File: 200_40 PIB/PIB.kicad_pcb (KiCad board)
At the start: 2 copper layers, 80 x 49 mm, 110 parts, among them Q1 3300V, Q3 VO3120, Q6 ?, Q7 ?, T2 Arthur, T3 Arthur, U2 L298N, U4 LM5022MM, U5 LTV-817-C, U6 TLVH431BQDCKT, U7 LM5022MM, U8 LTV-817-C, U9 TLVH431BQDCKT

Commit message: intermediate pib work, add history to gitignore
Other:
- board size 80 x 49 mm -> 18.3 x 25.4 mm
- board text added: "For Instructional Use Only."
- board text added: "SOLIDWORKS Educational Product."

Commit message: pretty pib that doesnt work
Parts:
- removed A1: Arduino_Nano_v3.x, Module:Arduino_Nano
- removed C1: 0.47uF, Capacitor_THT:C_Rect_L41.5mm_W13.0mm_P37.50mm_MKS4
- removed C26, C39: 100nF, Capacitor_SMD:C_2220_5750Metric
- removed Q1: 3300V, Package_TO_SOT_THT:TO-247-4_Horizontal_TabDown
- removed Q6, Q7: ?, Package_TO_SOT_THT:TO-247-4_Horizontal_TabDown
- removed T2, T3: Arthur, PlanarTransformer:40-2Transformer
- removed TP15, TP16, TP17, TP18, TP19, TP20, TP21, TP22, TP23, TP24, TP25, TP26, TP27, TP28, TP29, TP30, TP31, TP32, TP33, TP34, TP35, TP36, TP37, TP38, TP39, TP40, TP41, TP42, TP43, TP44: 5004, TestPoint:TestPoint_Keystone_5000-5004_Miniature
- removed U2: L298N, Package_TO_SOT_THT:TO-220-15_P2.54x5.08mm_StaggerOdd_Lead4.58mm_Vertical
- added J3: PIB Interface, Connector_Harwin:Harwin_Gecko_G125-MS12605M2P_2x13_P1.25mm_Vertical, F.Cu at (190.2, 112.7)
- added Q2: EPC2302, EPC_FETs:D0606F_100V, B.Cu at (221.0, 128.5)
- added Q4: EPC2302, EPC_FETs:D0606F_100V, B.Cu at (205.9, 128.6)
- added Q8: IRF7403, Package_SO:SOIC-8_3.9x4.9mm_P1.27mm, B.Cu at (209.5, 106.0)
- added Q9: IRF7403, Package_SO:SOIC-8_3.9x4.9mm_P1.27mm, B.Cu at (209.5, 100.5)
- added REF**: Transformer_NF_ETAL_P1165, Transformer_THT:Transformer_NF_ETAL_P1165, F.Cu at (230.0, 123.5)
- added REF**: TO-247-4_Horizontal_TabUp, Package_TO_SOT_THT:TO-247-4_Horizontal_TabUp, B.Cu at (244.6, 113.6)
- added REF**: Molex_PicoBlade_53261-0671_1x06-1MP_P1.25mm_Horizontal, Connector_Molex:Molex_PicoBlade_53261-0671_1x06-1MP_P1.25mm_Horizontal, F.Cu at (222.6, 94.7)
- added REF**: Transformer_NF_ETAL_P1165, Transformer_THT:Transformer_NF_ETAL_P1165, F.Cu at (209.5, 123.5)
- added REF**: MountingHole_3.2mm_M3_DIN965_Pad, MountingHole:MountingHole_3.2mm_M3_DIN965_Pad, F.Cu at (190.0, 130.5)
- added REF**: HARWIN_M80-5100442, PIB_Footprint_Library:HARWIN_M80-5100442, F.Cu at (207.0, 95.0)
- added REF**: MountingHole_3.2mm_M3_DIN965_Pad, MountingHole:MountingHole_3.2mm_M3_DIN965_Pad, F.Cu at (255.5, 137.0)
- added REF**: MountingHole_3.2mm_M3_DIN965_Pad, MountingHole:MountingHole_3.2mm_M3_DIN965_Pad, F.Cu at (196.5, 95.0)
- added REF**: Molex_PicoBlade_53261-0671_1x06-1MP_P1.25mm_Horizontal, Connector_Molex:Molex_PicoBlade_53261-0671_1x06-1MP_P1.25mm_Horizontal, F.Cu at (263.0, 125.5)
- added REF**: MountingHole_3.2mm_M3_DIN965_Pad, MountingHole:MountingHole_3.2mm_M3_DIN965_Pad, F.Cu at (256.5, 95.0)
- added U10: TLP3543, Package_DIP:DIP-6_W7.62mm, F.Cu at (247.7, 109.5)
- added U11: STM32G431KBTx, Package_QFP:LQFP-32_7x7mm_P0.8mm, F.Cu at (202.0, 106.5)
- added U12: DRV8220DRL, Package_TO_SOT_SMD:SOT-563, F.Cu at (209.5, 107.0)
- added U13: DRV8220DRL, Package_TO_SOT_SMD:SOT-563, F.Cu at (209.5, 103.5)
- added U3: BDJ2FC0WEFJ, Package_SO:HTSOP-8-1EP_3.9x4.9mm_P1.27mm_EP2.4x3.2mm, F.Cu at (216.5, 105.1)
- C16, C17, C18, C20, C22, C23, C24, C35, C36, C37, D4, D6, D7, D9, R17, R19, R22, R23, R24, R25, R33, R40, R43, R47, U4, U7: moved to B.Cu
- U1: value ~ -> ACS37042KLHBLT-030B3; footprint Package_SO:TSSOP-20_4.4x6.5mm_P0.65mm -> Package_TO_SOT_SMD:SOT-23-5_HandSoldering
- moved R29 188.1 mm to (260.2, 109.6)
- moved R20 181.4 mm to (260.1, 113.3), turned to 90 degrees
- moved R21 179.9 mm to (258.0, 113.3), turned to 90 degrees
- moved R30 158.2 mm to (259.5, 100.5)
- moved D5 151.8 mm to (231.5, 101.0), turned to 90 degrees
- moved R31 151.8 mm to (251.5, 100.5)
- moved Q3 151.0 mm to (242.8, 101.7), turned to -90 degrees
- moved U6 142.4 mm to (226.0, 100.5), turned to 90 degrees
- moved C19 139.9 mm to (246.0, 94.5), turned to 90 degrees
- moved C21 137.1 mm to (242.5, 94.5), turned to 90 degrees
- moved U5 128.6 mm to (231.7, 93.7)
- moved R36 126.4 mm to (245.4, 99.0)
- moved C15 123.0 mm to (230.2, 111.6)
- moved R35 122.1 mm to (242.0, 99.0)
- moved C14 118.5 mm to (225.5, 111.6)
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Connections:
- net /+18V_ISO renamed /+20V_ISO
- Q3 pad 2: /FIRE -> unconnected-(Q3-A-Pad2)
- Q3 pad 3: GNDPWR -> unconnected-(Q3-C-Pad3)
- R16 pad 2: Net-(U4-UVLO) -> /Igniter Supply/EN
- R18 pad 1: Net-(U4-UVLO) -> /Igniter Supply/EN
- U1 pad 1: unconnected-(U1-AV_DD-Pad1) -> GNDREF
- U1 pad 2: GNDPWR -> /I_IG
- U1 pad 3: unconnected-(U1-REFIN--Pad3) -> +3.3V
- U1 pad 4: unconnected-(U1-REFIN+/OUT-Pad4) -> /I_IG
- U1 pad 5: unconnected-(U1-CH0-Pad5) -> GNDPWR
- U4 pad 7: Net-(U4-UVLO) -> /Igniter Supply/EN
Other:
- board size 18.3 x 25.4 mm -> 80 x 49 mm
- board text removed: "For Instructional Use Only."
- board text removed: "SOLIDWORKS Educational Product."

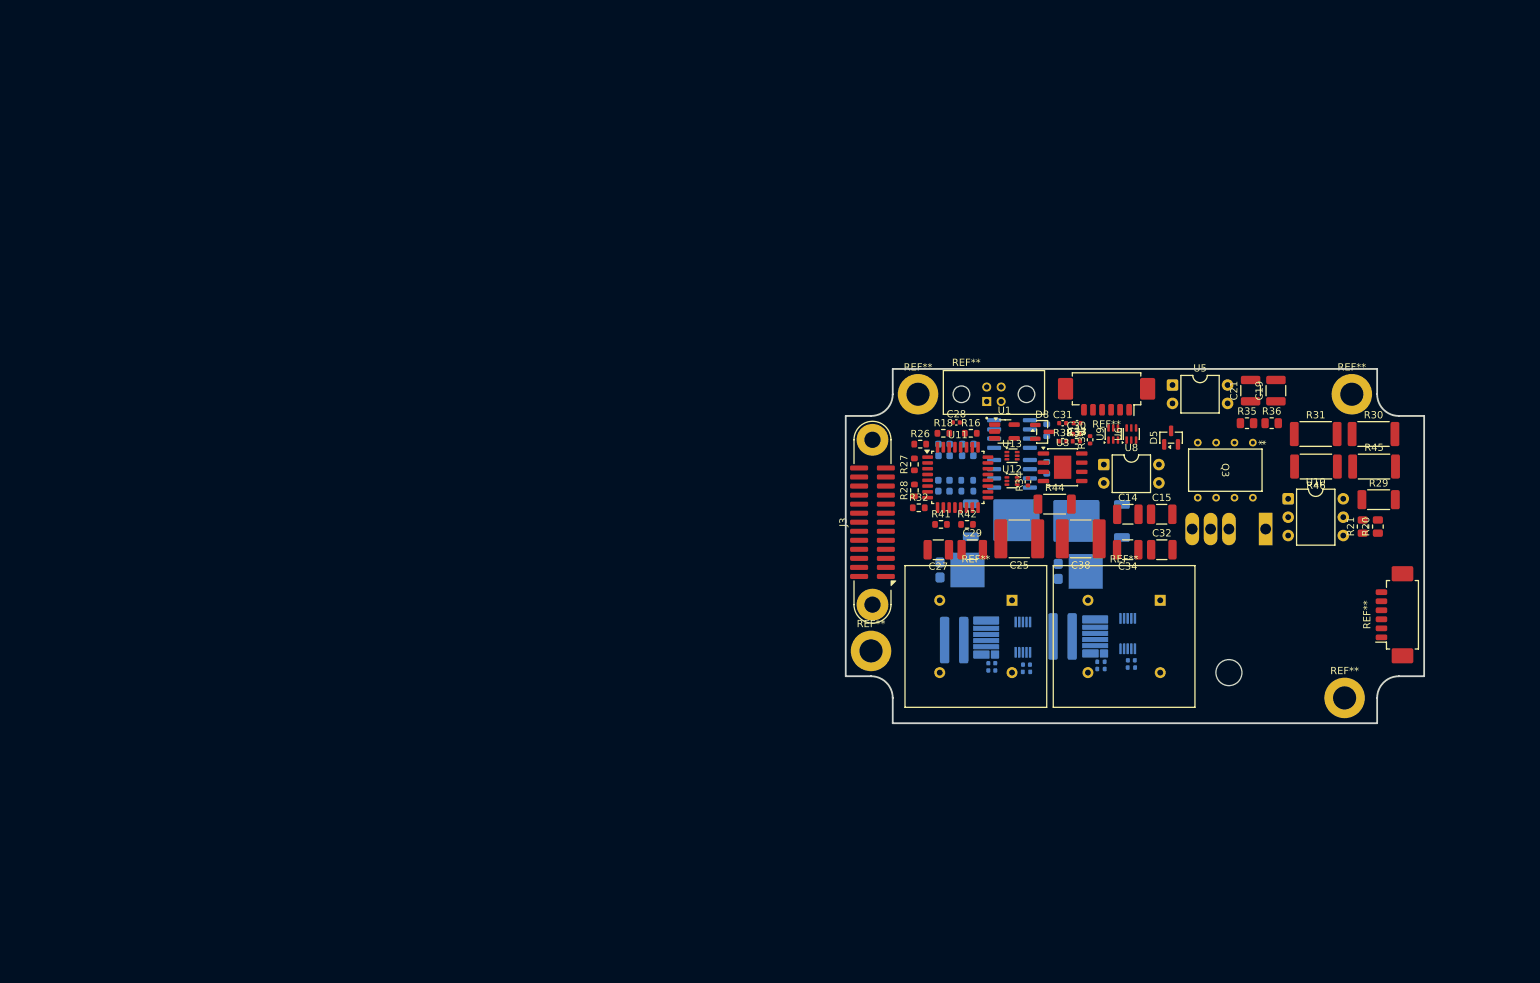
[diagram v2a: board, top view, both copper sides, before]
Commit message: assign PIB footprints, push ioc file to CubeMX 6.18.1
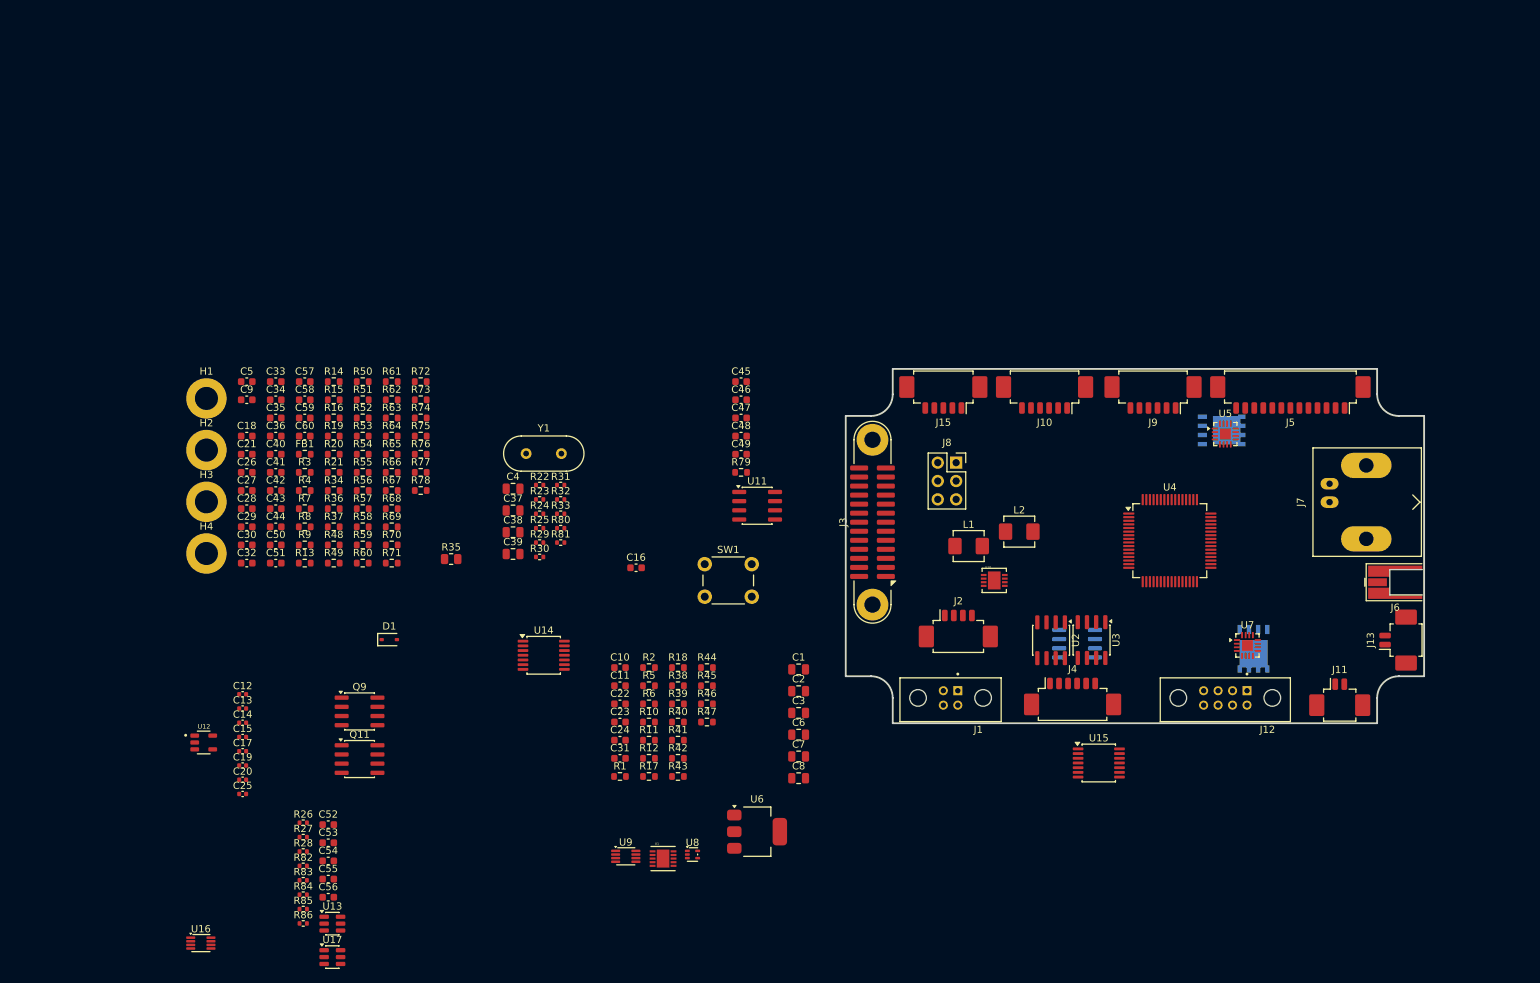
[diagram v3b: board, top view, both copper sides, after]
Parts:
- removed D4, D7: PPH10100, Package_TO_SOT_SMD:TO-277A
- removed D5, D8: BZX84C12, Package_TO_SOT_SMD:SOT-23
- removed D6, D9: VS-8EWS16STR-M3, Package_TO_SOT_SMD:TO-252-2
- removed Q3: VO3120, PIB_Footprint_Library:DIP_3120_VIS
- removed Q4: EPC2302, EPC_FETs:D0606F_100V
- removed Q8: IRF7403, Package_SO:SOIC-8_3.9x4.9mm_P1.27mm
- removed REF** (x2): Transformer_NF_ETAL_P1165, Transformer_THT:Transformer_NF_ETAL_P1165
- removed REF**: TO-247-4_Horizontal_TabUp, Package_TO_SOT_THT:TO-247-4_Horizontal_TabUp
- removed REF** (x2): Molex_PicoBlade_53261-0671_1x06-1MP_P1.25mm_Horizontal, Connector_Molex:Molex_PicoBlade_53261-0671_1x06-1MP_P1.25mm_Horizontal
- removed REF** (x4): MountingHole_3.2mm_M3_DIN965_Pad, MountingHole:MountingHole_3.2mm_M3_DIN965_Pad
- removed REF**: HARWIN_M80-5100442, PIB_Footprint_Library:HARWIN_M80-5100442
- added C1: 10uF, Capacitor_SMD:C_0805_2012Metric, F.Cu at (180.0, 133.1)
- added C10: 22nF, Capacitor_SMD:C_0603_1608Metric, F.Cu at (155.3, 132.8)
- added C11: 10nF, Capacitor_SMD:C_0603_1608Metric, F.Cu at (155.3, 135.3)
- added C12: 100nF, Capacitor_SMD:C_0402_1005Metric, F.Cu at (103.1, 136.5)
- added C13: 100nF, Capacitor_SMD:C_0402_1005Metric, F.Cu at (103.1, 138.5)
- added C2: 10uF, Capacitor_SMD:C_0805_2012Metric, F.Cu at (180.0, 136.1)
- added C26: 27pF, Capacitor_SMD:C_0603_1608Metric, F.Cu at (103.7, 105.8)
- added C3: 10uF, Capacitor_SMD:C_0805_2012Metric, F.Cu at (180.0, 139.1)
- added C39: 10uF, Capacitor_SMD:C_0805_2012Metric, F.Cu at (140.5, 117.1)
- added C4: 10uF, Capacitor_SMD:C_0805_2012Metric, F.Cu at (140.5, 108.1)
- added C40: 10nF, Capacitor_SMD:C_0603_1608Metric, F.Cu at (107.7, 103.3)
- added C41: 10nF, Capacitor_SMD:C_0603_1608Metric, F.Cu at (107.7, 105.8)
- added C42: 22pF, Capacitor_SMD:C_0603_1608Metric, F.Cu at (107.7, 108.3)
- added C43: 100nF, Capacitor_SMD:C_0603_1608Metric, F.Cu at (107.7, 110.8)
- added C44: 100nF, Capacitor_SMD:C_0603_1608Metric, F.Cu at (107.7, 113.3)
- added C45: TBD, Capacitor_SMD:C_0603_1608Metric, F.Cu at (172.0, 93.3)
- added C46: 10nF, Capacitor_SMD:C_0603_1608Metric, F.Cu at (172.0, 95.8)
- added C47: 1uF, Capacitor_SMD:C_0603_1608Metric, F.Cu at (172.0, 98.3)
- added C48: 1uF, Capacitor_SMD:C_0603_1608Metric, F.Cu at (172.0, 100.8)
- added C49: 10nF, Capacitor_SMD:C_0603_1608Metric, F.Cu at (172.0, 103.3)
- added C5: 100nF, Capacitor_SMD:C_0603_1608Metric, F.Cu at (103.7, 93.3)
- added C50: 100nF, Capacitor_SMD:C_0603_1608Metric, F.Cu at (107.7, 115.8)
- added C51: 100nF, Capacitor_SMD:C_0603_1608Metric, F.Cu at (107.7, 118.4)
- added C52: 100nF, Capacitor_SMD:C_0603_1608Metric, F.Cu at (114.9, 154.5)
- added C53: 100nF, Capacitor_SMD:C_0603_1608Metric, F.Cu at (114.9, 157.0)
- added C54: 100nF, Capacitor_SMD:C_0603_1608Metric, F.Cu at (114.9, 159.5)
- added C55: 1uF, Capacitor_SMD:C_0603_1608Metric, F.Cu at (114.9, 162.1)
- added C56: 1uF, Capacitor_SMD:C_0603_1608Metric, F.Cu at (114.9, 164.6)
- added C57: 100nF, Capacitor_SMD:C_0603_1608Metric, F.Cu at (111.7, 93.3)
- added C58: 100nF, Capacitor_SMD:C_0603_1608Metric, F.Cu at (111.7, 95.8)
- added C59: 100nF, Capacitor_SMD:C_0603_1608Metric, F.Cu at (111.7, 98.3)
- added C6: 10uF, Capacitor_SMD:C_0805_2012Metric, F.Cu at (180.0, 142.1)
- added C60: 100nF, Capacitor_SMD:C_0603_1608Metric, F.Cu at (111.7, 100.8)
- added C7: 10uF, Capacitor_SMD:C_0805_2012Metric, F.Cu at (180.0, 145.1)
- added C8: 10uF, Capacitor_SMD:C_0805_2012Metric, F.Cu at (180.0, 148.1)
- added C9: 4.7uF, Capacitor_SMD:C_0603_1608Metric, F.Cu at (103.7, 95.8)
- added D1: NSVR1020MW2T1G, Diode_SMD:D_SOD-323, F.Cu at (123.4, 128.9)
- added FB1: 120, Resistor_SMD:R_0603_1608Metric, F.Cu at (111.7, 103.3)
- added H1: M3, MountingHole:MountingHole_3.2mm_M3_DIN965_Pad, F.Cu at (98.1, 95.6)
- added H2: M3, MountingHole:MountingHole_3.2mm_M3_DIN965_Pad, F.Cu at (98.1, 102.7)
- added H3: M3, MountingHole:MountingHole_3.2mm_M3_DIN965_Pad, F.Cu at (98.1, 109.9)
- added H4: M3, MountingHole:MountingHole_3.2mm_M3_DIN965_Pad, F.Cu at (98.1, 117.0)
- added J1: M80-5100442, 0_PAY_Footprint_Library:HARWIN_M80-5100442, F.Cu at (201.0, 137.0)
- added J10: 53261-0671, Connector_Molex:Molex_PicoBlade_53261-0671_1x06-1MP_P1.25mm_Horizontal, F.Cu at (214.0, 94.5)
- added J11: 53261-0271, Connector_Molex:Molex_PicoBlade_53261-0271_1x02-1MP_P1.25mm_Horizontal, F.Cu at (254.8, 137.5)
- added J12: M80-5100842, 0_PAY_Footprint_Library:HARWIN_M80-5100842, F.Cu at (239.0, 137.0)
- added J13: 53261-0271, Connector_Molex:Molex_PicoBlade_53261-0271_1x02-1MP_P1.25mm_Horizontal, F.Cu at (263.5, 129.0)
- added J15: 53261-0571, Connector_Molex:Molex_PicoBlade_53261-0571_1x05-1MP_P1.25mm_Horizontal, F.Cu at (200.0, 94.5)
- added J2: 53261-0471, Connector_Molex:Molex_PicoBlade_53261-0471_1x04-1MP_P1.25mm_Horizontal, F.Cu at (202.1, 128.0)
- added J4: 53261-0671, Connector_Molex:Molex_PicoBlade_53261-0671_1x06-1MP_P1.25mm_Horizontal, F.Cu at (217.9, 137.4)
- added J5: 53261-1371, Connector_Molex:Molex_PicoBlade_53261-1371_1x13-1MP_P1.25mm_Horizontal, F.Cu at (248.0, 94.5)
- added J6: MMCX, Connector_Coaxial:MMCX_Molex_73415-0961_Horizontal_1.6mm-PCB, F.Cu at (262.5, 121.0)
- added J7: BNC, Connector_Coaxial:BNC_Amphenol_B6252HB-NPP3G-50_Horizontal, F.Cu at (253.4, 109.9)
- added J8: SWD/DEBUG, Connector_PinSocket_2.54mm:PinSocket_2x03_P2.54mm_Vertical, F.Cu at (201.8, 104.5)
- added J9: 53261-0671, Connector_Molex:Molex_PicoBlade_53261-0671_1x06-1MP_P1.25mm_Horizontal, F.Cu at (229.0, 94.5)
- added L1: 4.7uH, Inductor_SMD:L_Vishay_IHLP-1616, F.Cu at (203.5, 116.0)
- added L2: 4.7uH, Inductor_SMD:L_Vishay_IHLP-1616, F.Cu at (210.5, 114.0)
- added Q1: Si7489DP, Package_SO:PowerPAK_SO-8_Single, B.Cu at (242.9, 130.2)
- added Q10: IRF7832, Package_SO:SOIC-8_3.9x4.9mm_P1.27mm, B.Cu at (218.5, 129.5)
- added Q11: IRF7832, Package_SO:SOIC-8_3.9x4.9mm_P1.27mm, F.Cu at (119.3, 145.5)
- added R1: 100K, Resistor_SMD:R_0603_1608Metric, F.Cu at (155.3, 147.9)
- added R10: 1K, Resistor_SMD:R_0603_1608Metric, F.Cu at (159.3, 140.3)
- added R11: 1K, Resistor_SMD:R_0603_1608Metric, F.Cu at (159.3, 142.8)
- added R12: 1K, Resistor_SMD:R_0603_1608Metric, F.Cu at (159.3, 145.4)
- added R13: 4.7K, Resistor_SMD:R_0603_1608Metric, F.Cu at (111.7, 118.4)
- added R14: 4.7K, Resistor_SMD:R_0603_1608Metric, F.Cu at (115.7, 93.3)
- added R15: 100, Resistor_SMD:R_0603_1608Metric, F.Cu at (115.7, 95.8)
- added R2: 1K, Resistor_SMD:R_0603_1608Metric, F.Cu at (159.3, 132.8)
- added R3: 22K, Resistor_SMD:R_0603_1608Metric, F.Cu at (111.7, 105.8)
- added R4: 22K, Resistor_SMD:R_0603_1608Metric, F.Cu at (111.7, 108.3)
- added R48: 2K, Resistor_SMD:R_0603_1608Metric, F.Cu at (115.7, 115.8)
- added R49: 1K, Resistor_SMD:R_0603_1608Metric, F.Cu at (115.7, 118.4)
- added R5: 1K, Resistor_SMD:R_0603_1608Metric, F.Cu at (159.3, 135.3)
- added R50: 33K, Resistor_SMD:R_0603_1608Metric, F.Cu at (119.7, 93.3)
- added R51: 0R, Resistor_SMD:R_0603_1608Metric, F.Cu at (119.7, 95.8)
- added R52: 10K, Resistor_SMD:R_0603_1608Metric, F.Cu at (119.7, 98.3)
- added R53: 100K, Resistor_SMD:R_0603_1608Metric, F.Cu at (119.7, 100.8)
- added R54: 1K, Resistor_SMD:R_0603_1608Metric, F.Cu at (119.7, 103.3)
- added R55: 10K, Resistor_SMD:R_0603_1608Metric, F.Cu at (119.7, 105.8)
- added R56: 10K, Resistor_SMD:R_0603_1608Metric, F.Cu at (119.7, 108.3)
- added R57: 33K, Resistor_SMD:R_0603_1608Metric, F.Cu at (119.7, 110.8)
- added R58: 10K, Resistor_SMD:R_0603_1608Metric, F.Cu at (119.7, 113.3)
- added R59: 33K, Resistor_SMD:R_0603_1608Metric, F.Cu at (119.7, 115.8)
- added R6: 100K, Resistor_SMD:R_0603_1608Metric, F.Cu at (159.3, 137.8)
- added R60: 1K, Resistor_SMD:R_0603_1608Metric, F.Cu at (119.7, 118.4)
- added R61: 2K, Resistor_SMD:R_0603_1608Metric, F.Cu at (123.7, 93.3)
- added R62: 10K, Resistor_SMD:R_0603_1608Metric, F.Cu at (123.7, 95.8)
- added R63: 100K, Resistor_SMD:R_0603_1608Metric, F.Cu at (123.7, 98.3)
- added R64: 0R, Resistor_SMD:R_0603_1608Metric, F.Cu at (123.7, 100.8)
- added R65: 100m, Resistor_SMD:R_0603_1608Metric, F.Cu at (123.7, 103.3)
- added R66: 33K, Resistor_SMD:R_0603_1608Metric, F.Cu at (123.7, 105.8)
- added R67: 10K, Resistor_SMD:R_0603_1608Metric, F.Cu at (123.7, 108.3)
- added R68: 10K, Resistor_SMD:R_0603_1608Metric, F.Cu at (123.7, 110.8)
- added R69: 1K, Resistor_SMD:R_0603_1608Metric, F.Cu at (123.7, 113.3)
- added R7: 100K, Resistor_SMD:R_0603_1608Metric, F.Cu at (111.7, 110.8)
- added R70: 10K, Resistor_SMD:R_0603_1608Metric, F.Cu at (123.7, 115.8)
- added R71: 10K, Resistor_SMD:R_0603_1608Metric, F.Cu at (123.7, 118.4)
- added R72: 10K, Resistor_SMD:R_0603_1608Metric, F.Cu at (127.7, 93.3)
- added R73: 10K, Resistor_SMD:R_0603_1608Metric, F.Cu at (127.7, 95.8)
- added R74: 100K, Resistor_SMD:R_0603_1608Metric, F.Cu at (127.7, 98.3)
- added R75: 60.4K, Resistor_SMD:R_0603_1608Metric, F.Cu at (127.7, 100.8)
- added R76: 10K, Resistor_SMD:R_0603_1608Metric, F.Cu at (127.7, 103.3)
- added R77: 10K, Resistor_SMD:R_0603_1608Metric, F.Cu at (127.7, 105.8)
- added R78: 10K, Resistor_SMD:R_0603_1608Metric, F.Cu at (127.7, 108.3)
- added R79: TBD, Resistor_SMD:R_0603_1608Metric, F.Cu at (172.0, 105.8)
- added R8: 100K, Resistor_SMD:R_0603_1608Metric, F.Cu at (111.7, 113.3)
- added R80: 22, Resistor_SMD:R_0402_1005Metric, F.Cu at (147.1, 113.5)
- added R81: 22, Resistor_SMD:R_0402_1005Metric, F.Cu at (147.1, 115.5)
- added R82: 22, Resistor_SMD:R_0402_1005Metric, F.Cu at (111.5, 160.2)
- added R83: 22, Resistor_SMD:R_0402_1005Metric, F.Cu at (111.5, 162.2)
- added R84: 22, Resistor_SMD:R_0402_1005Metric, F.Cu at (111.5, 164.2)
- added R85: 22, Resistor_SMD:R_0402_1005Metric, F.Cu at (111.5, 166.2)
- added R86: 22, Resistor_SMD:R_0402_1005Metric, F.Cu at (111.5, 168.2)
- added R9: 100K, Resistor_SMD:R_0603_1608Metric, F.Cu at (111.7, 115.8)
- added SW1: 6mm tact, Button_Switch_THT:SW_PUSH_6mm, F.Cu at (167.0, 118.5)
- added U14: 74HC08PW, Package_SO:TSSOP-14_4.4x5mm_P0.65mm, F.Cu at (144.7, 131.1)
- added U15: 74HC08PW, Package_SO:TSSOP-14_4.4x5mm_P0.65mm, F.Cu at (221.5, 146.0)
- added U16: 74LVC2G157DCU, Package_SO:VSSOP-8_2.3x2mm_P0.5mm, F.Cu at (97.3, 170.9)
- added U17: 74LVC1G18DBV, Package_TO_SOT_SMD:SOT-23-6, F.Cu at (115.5, 172.8)
- added U2: MIC4424YM, Package_SO:SOIC-8_3.9x4.9mm_P1.27mm, F.Cu at (214.9, 129.0)
- added Y1: ECS-80-18-4XDN, Crystal:Crystal_HC49-U_Vertical, F.Cu at (142.3, 103.2)
- C14, C15: value 22uF -> 100nF; footprint Capacitor_SMD:C_1210_3225Metric -> Capacitor_SMD:C_0402_1005Metric
- C16: value 100nF -> 4.7uF; footprint Capacitor_SMD:C_0402_1005Metric -> Capacitor_SMD:C_0603_1608Metric; moved to F.Cu
- C17: value 10nF -> 100nF; moved to F.Cu
- C18: footprint Capacitor_SMD:C_0402_1005Metric -> Capacitor_SMD:C_0603_1608Metric; moved to F.Cu
- C19: value 10uF -> 100nF; footprint Capacitor_SMD:C_1210_3225Metric -> Capacitor_SMD:C_0402_1005Metric
- C20: value 1nF -> 100nF; moved to F.Cu
- C21, C32: value 10uF -> 1uF; footprint Capacitor_SMD:C_1210_3225Metric -> Capacitor_SMD:C_0603_1608Metric
- C22, C35: value 100pF -> 10nF; moved to F.Cu
- C23, C36: value 100pF -> 100nF; moved to F.Cu
- C24: value 47nF -> 100nF; moved to F.Cu
- C25: footprint Capacitor_SMD:C_2220_5750Metric -> Capacitor_SMD:C_0402_1005Metric
- C27: value 22uF -> 27pF; footprint Capacitor_SMD:C_1210_3225Metric -> Capacitor_SMD:C_0603_1608Metric
- C28: value 100nF -> 1uF; footprint Capacitor_SMD:C_0402_1005Metric -> Capacitor_SMD:C_0603_1608Metric
- C29: value 22uF -> 10nF; footprint Capacitor_SMD:C_1210_3225Metric -> Capacitor_SMD:C_0603_1608Metric
- C30: footprint Capacitor_SMD:C_0402_1005Metric -> Capacitor_SMD:C_0603_1608Metric
- C31: value 1uF -> 100nF; footprint Capacitor_SMD:C_0402_1005Metric -> Capacitor_SMD:C_0603_1608Metric
- C33: value 1nF -> 1uF; footprint Capacitor_SMD:C_0402_1005Metric -> Capacitor_SMD:C_0603_1608Metric
- C34: value 10uF -> 10nF; footprint Capacitor_SMD:C_1210_3225Metric -> Capacitor_SMD:C_0603_1608Metric
- C37: value 47nF -> 10uF; footprint Capacitor_SMD:C_0603_1608Metric -> Capacitor_SMD:C_0805_2012Metric; moved to F.Cu
- C38: value 100nF -> 10uF; footprint Capacitor_SMD:C_2220_5750Metric -> Capacitor_SMD:C_0805_2012Metric
- J3: value PIB Interface -> G125-MS12605M2P
- Q2: value EPC2302 -> Si7489DP; footprint EPC_FETs:D0606F_100V -> Package_SO:PowerPAK_SO-8_Single
- Q9: value IRF7403 -> IRF7832; moved to F.Cu
- R16: value 33K -> 100
- R17: value 33K -> 1.13K; moved to F.Cu
- R18: value 3.9K -> 21.5K
- R19: value 68.1K -> 100; footprint Resistor_SMD:R_0402_1005Metric -> Resistor_SMD:R_0603_1608Metric; moved to F.Cu
- R20, R21: value 1K -> 100; footprint Resistor_SMD:R_0805_2012Metric -> Resistor_SMD:R_0603_1608Metric
- R22: value 3.3 -> 22; moved to F.Cu
- R23: value 1K -> 22; moved to F.Cu
- R24: value 100 -> 22; moved to F.Cu
- R25: value 100m -> 22; footprint Resistor_SMD:R_1225_3264Metric -> Resistor_SMD:R_0402_1005Metric; moved to F.Cu
- R26: value 100 -> 22; footprint Resistor_SMD:R_0603_1608Metric -> Resistor_SMD:R_0402_1005Metric
- R27: value 1K -> 22; footprint Resistor_SMD:R_0603_1608Metric -> Resistor_SMD:R_0402_1005Metric
- R28: value 10K -> 22; footprint Resistor_SMD:R_0603_1608Metric -> Resistor_SMD:R_0402_1005Metric
- R29: value 0 -> 100; footprint Resistor_SMD:R_2010_5025Metric -> Resistor_SMD:R_0402_1005Metric
- R30: value 402K -> 100; footprint Resistor_SMD:R_2512_6332Metric -> Resistor_SMD:R_0402_1005Metric
- R31: value 1M -> 100; footprint Resistor_SMD:R_2512_6332Metric -> Resistor_SMD:R_0402_1005Metric
- R32: value 3.12K -> 100; footprint Resistor_SMD:R_0603_1608Metric -> Resistor_SMD:R_0402_1005Metric
- R33: value 3.9K -> 100; footprint Resistor_SMD:R_0603_1608Metric -> Resistor_SMD:R_0402_1005Metric; moved to F.Cu
- R34: value 68.1K -> 100; footprint Resistor_SMD:R_0402_1005Metric -> Resistor_SMD:R_0603_1608Metric
- R35: value 1K -> 15m
- R36: value 1K -> 4.7K; footprint Resistor_SMD:R_0805_2012Metric -> Resistor_SMD:R_0603_1608Metric
- R37: value 3.3 -> 4.7K; footprint Resistor_SMD:R_0402_1005Metric -> Resistor_SMD:R_0603_1608Metric
- R38: footprint Resistor_SMD:R_0402_1005Metric -> Resistor_SMD:R_0603_1608Metric
- R39: value 100 -> 100K; footprint Resistor_SMD:R_0402_1005Metric -> Resistor_SMD:R_0603_1608Metric
- R40: value 100m -> 100K; footprint Resistor_SMD:R_1225_3264Metric -> Resistor_SMD:R_0603_1608Metric; moved to F.Cu
- R41: value 100 -> 100K
- R42: value 1K -> 100K
- R43: value 10K -> 1K; moved to F.Cu
- R44: value 0 -> 100K; footprint Resistor_SMD:R_2010_5025Metric -> Resistor_SMD:R_0603_1608Metric
- R45: value 402K -> 10K; footprint Resistor_SMD:R_2512_6332Metric -> Resistor_SMD:R_0603_1608Metric
- R46: value 1M -> 43K; footprint Resistor_SMD:R_2512_6332Metric -> Resistor_SMD:R_0603_1608Metric
- R47: value 3.12K -> 1K; moved to F.Cu
- U1: value ACS37042KLHBLT-030B3 -> LT3065EDDPBF; footprint Package_TO_SOT_SMD:SOT-23-5_HandSoldering -> 0_PAY_Footprint_Library:DFN-10_DD
- U10: value TLP3543 -> LT8580EDD; footprint Package_DIP:DIP-6_W7.62mm -> 0_PAY_Footprint_Library:DFN-8_DD
- U11: value STM32G431KBTx -> OP37; footprint Package_QFP:LQFP-32_7x7mm_P0.8mm -> Package_SO:SOIC-8_3.9x4.9mm_P1.27mm
- U12: value DRV8220DRL -> MAX823TEUK_T; footprint Package_TO_SOT_SMD:SOT-563 -> 0_PAY_Footprint_Library:SOT95P280X145-5N
- U13: value DRV8220DRL -> 74LVC1G18DBV; footprint Package_TO_SOT_SMD:SOT-563 -> Package_TO_SOT_SMD:SOT-23-6
- U3: value BDJ2FC0WEFJ -> MIC4424YM; footprint Package_SO:HTSOP-8-1EP_3.9x4.9mm_P1.27mm_EP2.4x3.2mm -> Package_SO:SOIC-8_3.9x4.9mm_P1.27mm
- U4: value LM5022MM -> STM32G431RBTx; footprint Package_SO:MSOP-10_3x3mm_P0.5mm -> Package_QFP:LQFP-64_10x10mm_P0.5mm; moved to F.Cu
- U5: value LTV-817-C -> ADM1270ACPZ; footprint Package_DIP:DIP-4_W7.62mm -> Package_CSP:LFCSP-16-1EP_3x3mm_P0.5mm_EP1.5x1.5mm
- U6: value TLVH431BQDCKT -> LM1117MP-3.3; footprint Package_TO_SOT_SMD:SOT-363_SC-70-6 -> Package_TO_SOT_SMD:SOT-223-3_TabPin2
- U7: value LM5022MM -> ADM1270ACPZ; footprint Package_SO:MSOP-10_3x3mm_P0.5mm -> Package_CSP:LFCSP-16-1EP_3x3mm_P0.5mm_EP1.5x1.5mm; moved to F.Cu
- U8: value LTV-817-C -> 74LVC1GU04DRL; footprint Package_DIP:DIP-4_W7.62mm -> Package_TO_SOT_SMD:SOT-553
- U9: value TLVH431BQDCKT -> 74LVC2G126DCU; footprint Package_TO_SOT_SMD:SOT-363_SC-70-6 -> Package_SO:VSSOP-8_2.3x2mm_P0.5mm
- moved C19 152.0 mm to (103.1, 146.3), turned to 0 degrees
- moved R20 144.8 mm to (115.7, 103.3), turned to 0 degrees
- moved R21 142.5 mm to (115.7, 105.8), turned to 0 degrees
- moved C21 139.1 mm to (103.7, 103.3), turned to 0 degrees
- moved C15 130.8 mm to (103.1, 142.4)
- moved R36 130.3 mm to (115.7, 110.8)
- moved C32 126.6 mm to (103.7, 118.4)
- moved C14 125.8 mm to (103.1, 140.4)
- moved C17 123.6 mm to (103.1, 144.4)
- moved C34 119.6 mm to (107.7, 95.8), turned to 0 degrees
- moved U12 117.5 mm to (97.7, 143.2)
- moved R30 116.6 mm to (144.2, 117.5)
- moved R29 116.2 mm to (144.2, 115.5)
- moved C30 115.8 mm to (103.7, 115.8)
- moved U13 114.1 mm to (115.5, 168.2)
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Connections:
- C14 pad 1: +BATT -> +3.3V
- C14 pad 2: GNDPWR -> GND
- C15 pad 1: +BATT -> +3.3V
- C15 pad 2: GNDPWR -> GND
- C16 pad 1: +6V -> +3.3V
- C16 pad 2: GNDPWR -> GND
- C17 pad 1: Net-(U4-SS) -> VDDA
- C17 pad 2: GNDPWR -> GND
- C18 pad 1: Net-(U4-VCC) -> VDDA
- C18 pad 2: GNDPWR -> GND
- C19 pad 1: +BATT -> /ADC_TANK_NTC_1
- C19 pad 2: /Igniter Supply/VSN -> GND
- C20 pad 1: Net-(C20-Pad1) -> /ADC_TANK_NTC_2
- C20 pad 2: GNDPWR -> GND
- C21 pad 1: +BATT -> Net-(U5-ISET)
- C21 pad 2: /Igniter Supply/VSN -> GND
- C22 pad 1: Net-(C22-Pad1) -> 12V
- C22 pad 2: +6V -> Net-(U1-ADJ/SENSE)
- C23 pad 1: Net-(C23-Pad1) -> +12V
- C23 pad 2: /Igniter Supply/VS -> GND
- C24 pad 1: Net-(U6-K) -> +12V
- C24 pad 2: Net-(U6-REF) -> GND
- C25 pad 1: GNDPWR -> VDDA
- C25 pad 2: -400V -> GND
- C27 pad 1: +BATT -> GND
- C27 pad 2: GNDPWR -> Net-(U4-PF1)
- C28 pad 1: +6V -> BAT_HOT
- C28 pad 2: GNDPWR -> GND
- C29 pad 1: +BATT -> Net-(U5-TIMER_OFF)
- C29 pad 2: GNDPWR -> GND
- C30 pad 1: Net-(U7-SS) -> Net-(U5-TIMER)
- C30 pad 2: GNDPWR -> GND
- C31 pad 1: Net-(U7-VCC) -> 3.3V_EGSE
- C31 pad 2: GNDPWR -> GND
- C32 pad 1: +BATT -> Net-(U7-ISET)
- C32 pad 2: /Discharge Supply/VSN -> GND
- C33 pad 1: Net-(C33-Pad1) -> BAT_HOT
- C33 pad 2: GNDPWR -> GND
- C34 pad 1: +BATT -> Net-(U7-TIMER_OFF)
- C34 pad 2: /Discharge Supply/VSN -> GND
- C35 pad 1: Net-(C35-Pad1) -> Net-(U7-TIMER)
- C35 pad 2: +6V -> GND
- C36 pad 1: Net-(C36-Pad1) -> Net-(U12-~{MR})
- C36 pad 2: /Discharge Supply/VS -> GND
- C37 pad 1: Net-(U9-K) -> GND
- C37 pad 2: Net-(U9-REF) -> -5V
- C38 pad 1: GNDPWR -> GND
- C38 pad 2: -400V -> -5V
- J3 pad 1: unconnected-(J3-Pin_1-Pad1) -> BAT_HOT
- J3 pad 11: Net-(J3-Pin_11) -> unconnected-(J3-Pin_11-Pad11)
- J3 pad 12: +3.3V -> +5V
- J3 pad 13: GNDPWR -> +5V
- J3 pad 14: unconnected-(J3-Pin_14-Pad14) -> GND
- J3 pad 15: unconnected-(J3-Pin_15-Pad15) -> GND
- J3 pad 16: unconnected-(J3-Pin_16-Pad16) -> GND
- J3 pad 17: unconnected-(J3-Pin_17-Pad17) -> GND
- J3 pad 18: unconnected-(J3-Pin_18-Pad18) -> GND
- J3 pad 19: /USART2_TX -> GND
- J3 pad 2: unconnected-(J3-Pin_2-Pad2) -> BAT_HOT
- J3 pad 20: /USART2_RX -> Net-(J3-Pin_20)
- J3 pad 21: /SCL -> Net-(J3-Pin_21)
- J3 pad 22: /SDA -> Net-(J3-Pin_22)
- J3 pad 23: /SWDIO -> Net-(J3-Pin_23)
- J3 pad 24: /SWDCLK -> Net-(J3-Pin_24)
- J3 pad 25: /FIRE -> GND
- J3 pad 26: GNDREF -> GND
- J3 pad 3: unconnected-(J3-Pin_3-Pad3) -> BAT_HOT
- J3 pad 4: unconnected-(J3-Pin_4-Pad4) -> +3.3V
- J3 pad 5: unconnected-(J3-Pin_5-Pad5) -> +3.3V
- J3 pad 6: unconnected-(J3-Pin_6-Pad6) -> /EXT_SPI_MISO
- J3 pad 7: unconnected-(J3-Pin_7-Pad7) -> /EXT_SPI_MOSI
- J3 pad 8: unconnected-(J3-Pin_8-Pad8) -> /EXT_SPI_SCK
- J3 pad 9: unconnected-(J3-Pin_9-Pad9) -> /EXT_SPI_~{CS}
- Q2 pad 1: Net-(Q2-G) -> Net-(U7-SENSE-)
- Q2 pad 2: /Igniter Supply/VS -> Net-(U7-SENSE-)
- Q2 pad 3: /Igniter Supply/VD -> Net-(U7-SENSE-)
- Q2 pad 4: /Igniter Supply/VS -> Net-(Q2-G)
- Q2 pad 5: /Igniter Supply/VD -> VBAT_IGN
- Q9 pad 1: GNDPWR -> GND
- Q9 pad 2: GNDPWR -> GND
- Q9 pad 3: GNDPWR -> GND
- R16 pad 1: +BATT -> /INT_I2C_SCL
- R16 pad 2: /Igniter Supply/EN -> Net-(J15-Pin_2)
- R17 pad 1: +BATT -> Net-(U1-ADJ/SENSE)
- R17 pad 2: Net-(U7-UVLO) -> GND
- R18 pad 1: /Igniter Supply/EN -> 12V
- R18 pad 2: GNDPWR -> Net-(U1-ADJ/SENSE)
- R19 pad 1: Net-(U4-RT) -> /HTR2_EN
- R19 pad 2: GNDPWR -> Net-(Q9-G)
- R20 pad 1: +BATT -> /SWDCLK
- R20 pad 2: /Igniter Supply/VSN -> Net-(U4-PA14)
- R21 pad 1: +BATT -> /SWDIO
- R21 pad 2: /Igniter Supply/VSN -> Net-(U4-PA13)
- R22 pad 1: Net-(U4-OUT) -> /EXT_SPI_~{CS}
- R22 pad 2: Net-(Q2-G) -> Net-(U4-PA4)
- R23 pad 1: Net-(U4-CS) -> /EXT_SPI_SCK
- R23 pad 2: Net-(C20-Pad1) -> Net-(U4-PA5)
- R24 pad 1: Net-(C20-Pad1) -> /EXT_SPI_MISO
- R24 pad 2: /Igniter Supply/VS -> Net-(U4-PA6)
- R25 pad 1: /Igniter Supply/VS -> /EXT_SPI_MOSI
- R25 pad 2: GNDPWR -> Net-(U4-PA7)
- R26 pad 1: /Igniter Supply/VD -> /DPT MUX/TANK_SCK
- R26 pad 2: Net-(C23-Pad1) -> Net-(J9-Pin_3)
- R27 pad 1: Net-(C22-Pad1) -> /DPT MUX/TANK_DOUT
- R27 pad 2: /Igniter Supply/FB -> Net-(J9-Pin_4)
- R28 pad 1: /Igniter Supply/FB -> /DPT MUX/TANK_DIN
- R28 pad 2: GNDPWR -> Net-(J9-Pin_5)
- R29 pad 1: GNDPWR -> /IGNITER
- R29 pad 2: GNDPWR -> Net-(J3-Pin_22)
- R30 pad 1: Net-(D5-K) -> /DRDY
- R30 pad 2: GNDPWR -> Net-(J3-Pin_23)
- R31 pad 1: GNDPWR -> /ARM/~{SAFE}
- R31 pad 2: Net-(U6-REF) -> Net-(J3-Pin_24)
- R32 pad 1: Net-(U6-REF) -> /EXT_I2C_SCL
- R32 pad 2: -400V -> Net-(J3-Pin_20)
- R33 pad 1: Net-(U7-UVLO) -> /EXT_I2C_SDA
- R33 pad 2: GNDPWR -> Net-(J3-Pin_21)
- R34 pad 1: Net-(U7-RT) -> /HTR1_EN
- R34 pad 2: GNDPWR -> Net-(Q11-G)
- R35 pad 1: +BATT -> Net-(U5-SENSE-)
- R35 pad 2: /Discharge Supply/VSN -> BAT_HOT
- R36 pad 1: +BATT -> /EXT_I2C_SCL
- R36 pad 2: /Discharge Supply/VSN -> +3.3V
- R37 pad 1: Net-(U7-OUT) -> /EXT_I2C_SDA
- R37 pad 2: Net-(Q4-G) -> +3.3V
- R38 pad 1: Net-(U7-CS) -> /VALVE1_H_GATED
- R38 pad 2: Net-(C33-Pad1) -> Net-(U2-INB)
- R39 pad 1: Net-(C33-Pad1) -> Net-(U2-INB)
- R39 pad 2: /Discharge Supply/VS -> GND
- R40 pad 1: /Discharge Supply/VS -> Net-(U2-INA)
- R40 pad 2: GNDPWR -> GND
- R41 pad 1: /Discharge Supply/VD -> Net-(U3-INB)
- R41 pad 2: Net-(C36-Pad1) -> GND
- R42 pad 1: Net-(C35-Pad1) -> Net-(U3-INA)
- R42 pad 2: /Discharge Supply/FB -> GND
- R43 pad 1: /Discharge Supply/FB -> /OPEN/~{CLOSE}
- R43 pad 2: GNDPWR -> Net-(R43-Pad2)
- R44 pad 1: GNDPWR -> Net-(R43-Pad2)
- R44 pad 2: GNDPWR -> GND
- R45 pad 1: Net-(D8-K) -> GND
- R45 pad 2: GNDPWR -> Net-(R45-Pad2)
- R46 pad 1: GNDPWR -> Net-(R45-Pad2)
- R46 pad 2: Net-(U9-REF) -> 12V_GSE
- R47 pad 1: Net-(U9-REF) -> /OPEN/~{CLOSE}
- R47 pad 2: -400V -> Net-(Q10-G)
- U1 pad 1: GNDREF -> BAT_HOT
- U1 pad 2: /I_IG -> BAT_HOT
- U1 pad 3: +3.3V -> BAT_HOT
- U1 pad 4: /I_IG -> Net-(U1-PWRGD)
- U1 pad 5: GNDPWR -> Net-(U1-IMAX)
- U10 pad 1: unconnected-(U10-Pad1) -> Net-(U10-FBX)
- U10 pad 2: GNDPWR -> Net-(U10-VC)
- U10 pad 3: unconnected-(U10-Pad3) -> +5V
- U10 pad 4: Net-(F3-Pad2) -> Net-(U10-SW)
- U10 pad 5: Net-(J3-Pin_11) -> Net-(U10-~{SHDN})
- U10 pad 6: Net-(F3-Pad2) -> Net-(U10-RT)
- U11 pad 1: +3.3V -> unconnected-(U11B-VOSADJ-Pad1)
- U11 pad 2: /Igniter Supply/V_CTRL -> Net-(U11A--)
- U11 pad 3: /Discharge Supply/EN -> GND
- U11 pad 4: /RESET -> -5V
- U11 pad 5: /V_MAIN -> unconnected-(U11B-NC-Pad5)
- U11 pad 6: /V_IG -> /ADC_I_DCHG
- U11 pad 7: /USART2_TX -> +5V
- U11 pad 8: /USART2_RX -> unconnected-(U11B-VOSADJ-Pad8)
- U12 pad 1: /Valve Driver/LHL1 -> /nRST
- U12 pad 2: /Valve Driver/LHL2 -> GND
- U12 pad 3: GNDPWR -> Net-(U12-~{MR})
- U12 pad 4: Net-(U12-OUT2) -> /WDG_IN
- U12 pad 5: +12V -> +3.3V
- U13 pad 1: /Valve Driver/LHL3 -> /FRIT/~{TANK}
- U13 pad 2: /Valve Driver/LHL4 -> GND
- U13 pad 3: GNDPWR -> /INT_SPI_MOSI
- U13 pad 4: Net-(U13-OUT2) -> /DPT MUX/FRIT_DIN
- U13 pad 5: +12V -> +3.3V
- U13 pad 6: Net-(U13-OUT1) -> /DPT MUX/TANK_DIN
- U3 pad 1: +12V -> (no net)
- U3 pad 2: unconnected-(U3-NC-Pad2) -> Net-(U3-INA)
- U3 pad 3: GNDPWR -> GND
- U3 pad 4: unconnected-(U3-NC-Pad4) -> Net-(U3-INB)
- U3 pad 5: Net-(J3-Pin_11) -> Net-(J4-Pin_4)
- U3 pad 6: unconnected-(U3-NC-Pad6) -> +12V
- U3 pad 7: unconnected-(U3-NC-Pad7) -> Net-(J4-Pin_3)
- U3 pad 8: Net-(J3-Pin_11) -> (no net)
- U4 pad 1: +6V -> +3.3V
- U4 pad 10: Net-(U4-SS) -> /ADC_I_IGN_PK
- U4 pad 2: /Igniter Supply/FB -> /DISCHARGE_PGOOD
- U4 pad 3: unconnected-(U4-COMP-Pad3) -> /IGNITER_PGOOD
- U4 pad 4: Net-(U4-VCC) -> unconnected-(U4-PC15-Pad4)
- U4 pad 5: Net-(U4-OUT) -> Net-(U4-PF0)
- U4 pad 6: GNDPWR -> Net-(U4-PF1)
- U4 pad 7: /Igniter Supply/EN -> /nRST
- U4 pad 8: Net-(U4-CS) -> Net-(U4-PC0)
- U4 pad 9: Net-(U4-RT) -> Net-(U4-PC1)
- U5 pad 1: Net-(D5-K) -> Net-(U5-ISET)
- U5 pad 2: Net-(U6-K) -> Net-(U5-ISET)
- U5 pad 3: Net-(C22-Pad1) -> Net-(U5-UV)
- U5 pad 4: +6V -> Net-(U5-OV)
- U6 pad 1: Net-(U6-K) -> GND
- U6 pad 2: (no net) -> 3.3V_EGSE
- U6 pad 3: Net-(U6-REF) -> 12V_GSE
- U7 pad 1: +6V -> Net-(U7-ISET)
- U7 pad 10: Net-(U7-SS) -> Net-(U7-FB_PG)
- U7 pad 2: /Discharge Supply/FB -> Net-(U7-ISET)
- U7 pad 3: unconnected-(U7-COMP-Pad3) -> Net-(U7-UV)
- U7 pad 4: Net-(U7-VCC) -> Net-(U7-OV)
- U7 pad 5: Net-(U7-OUT) -> Net-(U7-ENABLE)
- U7 pad 6: GNDPWR -> Net-(U7-~{FAULT})
- U7 pad 7: Net-(U7-UVLO) -> GND
- U7 pad 8: Net-(U7-CS) -> Net-(U7-TIMER)
- U7 pad 9: Net-(U7-RT) -> Net-(U7-TIMER_OFF)
- U8 pad 1: Net-(D8-K) -> unconnected-(U8-NC-Pad1)
- U8 pad 2: Net-(U9-K) -> Net-(R43-Pad2)
- U8 pad 3: Net-(C35-Pad1) -> GND
- U8 pad 4: +6V -> Net-(U8-Pad4)
- U9 pad 1: Net-(U9-K) -> Net-(R45-Pad2)
- U9 pad 2: (no net) -> Net-(R43-Pad2)
- U9 pad 3: Net-(U9-REF) -> Net-(U3-INA)
- U9 pad 4: (no net) -> GND
- U9 pad 5: (no net) -> Net-(U8-Pad4)
- U9 pad 6: -400V -> Net-(U3-INB)
